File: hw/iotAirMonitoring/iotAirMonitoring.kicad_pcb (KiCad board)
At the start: 2 copper layers, 100 x 100 mm, 122 parts, among them J1 MQ-7, J10 USB_DATA, J11 PWR, J12 USB_B_Micro, J13 PM1003, J2 VEML7700, J3 SHT40, J4 PROGRAMMER, J5 ML8511, J6 EN_3V3_PROGRAMMER, J7 BMP388, J8 PMS5003, J9 USB_C_Receptacle_USB2.0, Q1 MMBT3904, Q10 AO3401A, Q11 2N7002, Q12 AO3401A, Q13 2N7002, Q14 AO3401A, Q15 2N7002, Q16 2N7002, Q17 2N7002, Q2 MMBT3904, Q3 AO3401A, Q4 2N7002, Q5 AO3401A, Q6 2N7002, Q7 AO3401A, Q8 2N7002, Q9 AO3401A, SW1 PWR_ON, SW2 PWR_OFF, SW3 RESET, SW4 SW_Push, U1 ESP32-WROOM-32, U2 MCP3202-BI/SN, U3 AMS1117-3.3, U4 TPS54331, U5 RFM95W-868S2

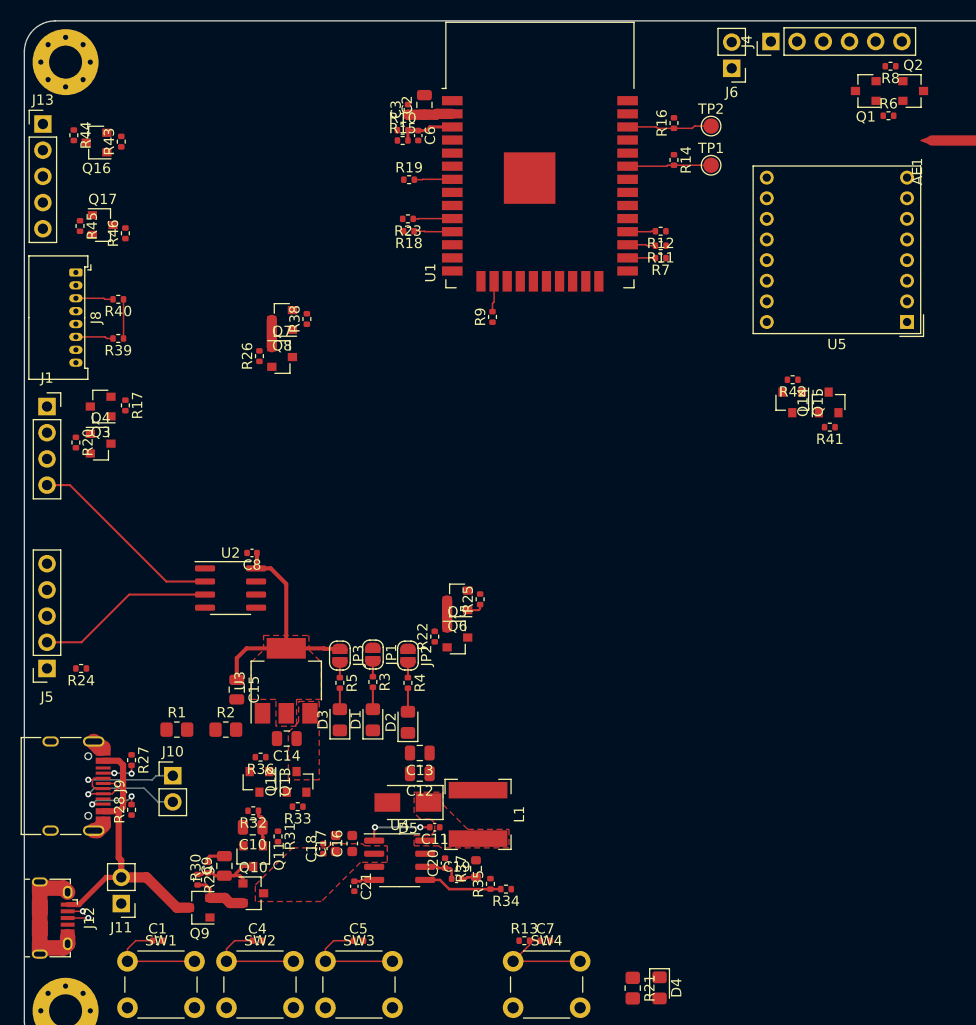
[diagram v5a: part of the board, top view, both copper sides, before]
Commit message: More routing on main board
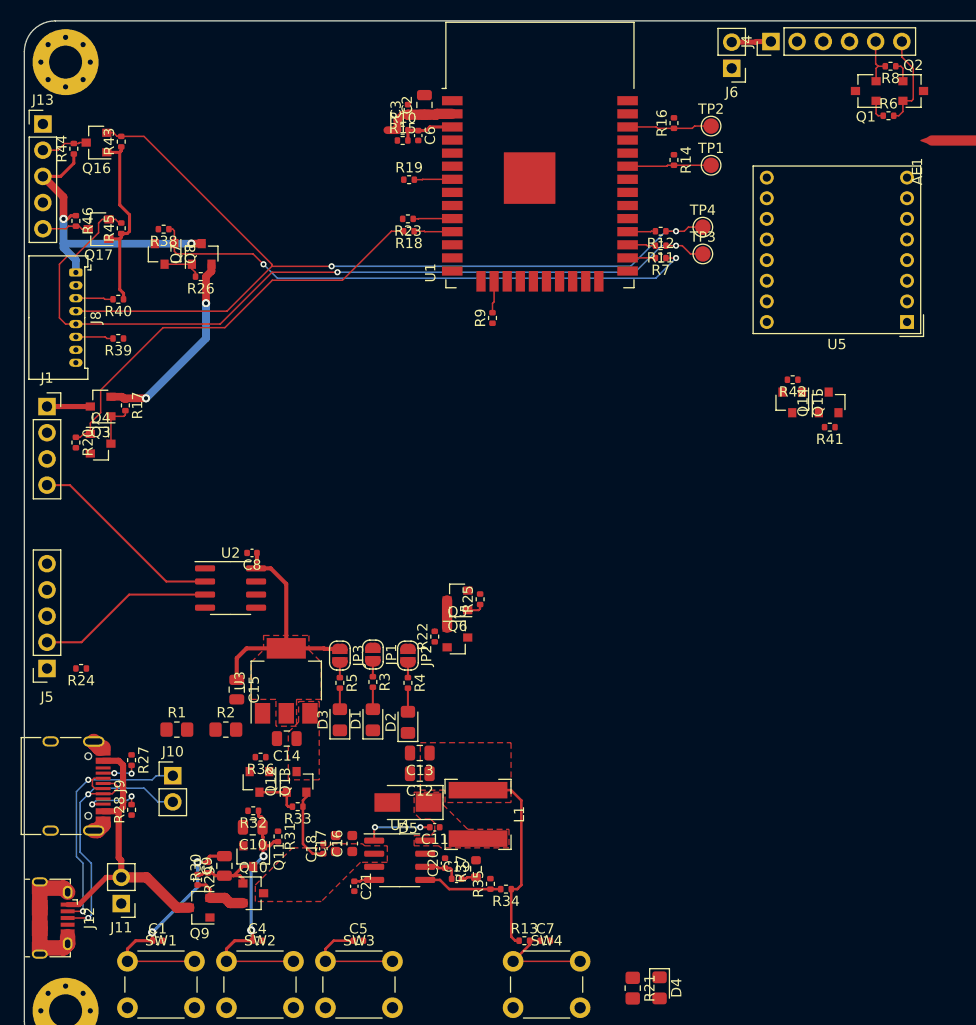
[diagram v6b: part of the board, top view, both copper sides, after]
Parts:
- added TP3: TP_RX1, TestPoint:TestPoint_Pad_D1.5mm, F.Cu at (221.8, 67.6)
- added TP4: TP_TX1, TestPoint:TestPoint_Pad_D1.5mm, F.Cu at (221.8, 65.0)
- moved R38 16.4 mm to (169.5, 65.2), turned to 180 degrees
- moved Q8 13.1 mm to (169.6, 67.6), turned to 270 degrees
- moved Q7 12.7 mm to (173.2, 67.6), turned to 90 degrees
- moved R26 9.58 mm to (173.1, 69.8), turned to 180 degrees
- moved R46 4.95 mm to (161.0, 64.4), turned to 270 degrees
- moved R45 4.01 mm to (165.4, 65.1), turned to 90 degrees
- moved R44 1.31 mm to (160.8, 57.4), turned to 90 degrees
- moved Q17 0.57 mm to (163.2, 65.2), turned to 180 degrees
- moved R9 0.10 mm to (201.4, 73.8)
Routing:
- net TX1: track 0.00 -> 86.6 mm, vias 0 -> 2
- net RX1: track 0.00 -> 80.8 mm, vias 0 -> 2
- net PMS_EN: track 0.00 -> 54.1 mm, vias 0 -> 2
- net Net-(Q4-Pad1): track 0.00 -> 42.0 mm
- net 3V3: track 8.14 -> 45.5 mm
- net DUST_VDD: track 0.00 -> 29.8 mm, vias 0 -> 2
- net VDD: track 0.00 -> 27.1 mm, vias 0 -> 2
- net D-: track 13.1 -> 26.6 mm
- net D+: track 15.8 -> 28.7 mm
- net PWR_OFF: track 14.3 -> 25.6 mm, vias 0 -> 2
- net PWR_ON: track 12.6 -> 23.0 mm, vias 0 -> 2
- net RTS: track 0.00 -> 9.22 mm
- net DTR: track 0.00 -> 4.72 mm
- net PM_RX: track 0.00 -> 4.62 mm
- net Net-(Q3-Pad1): track 0.00 -> 4.51 mm
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- added copper zone on F.Cu, net 3V3

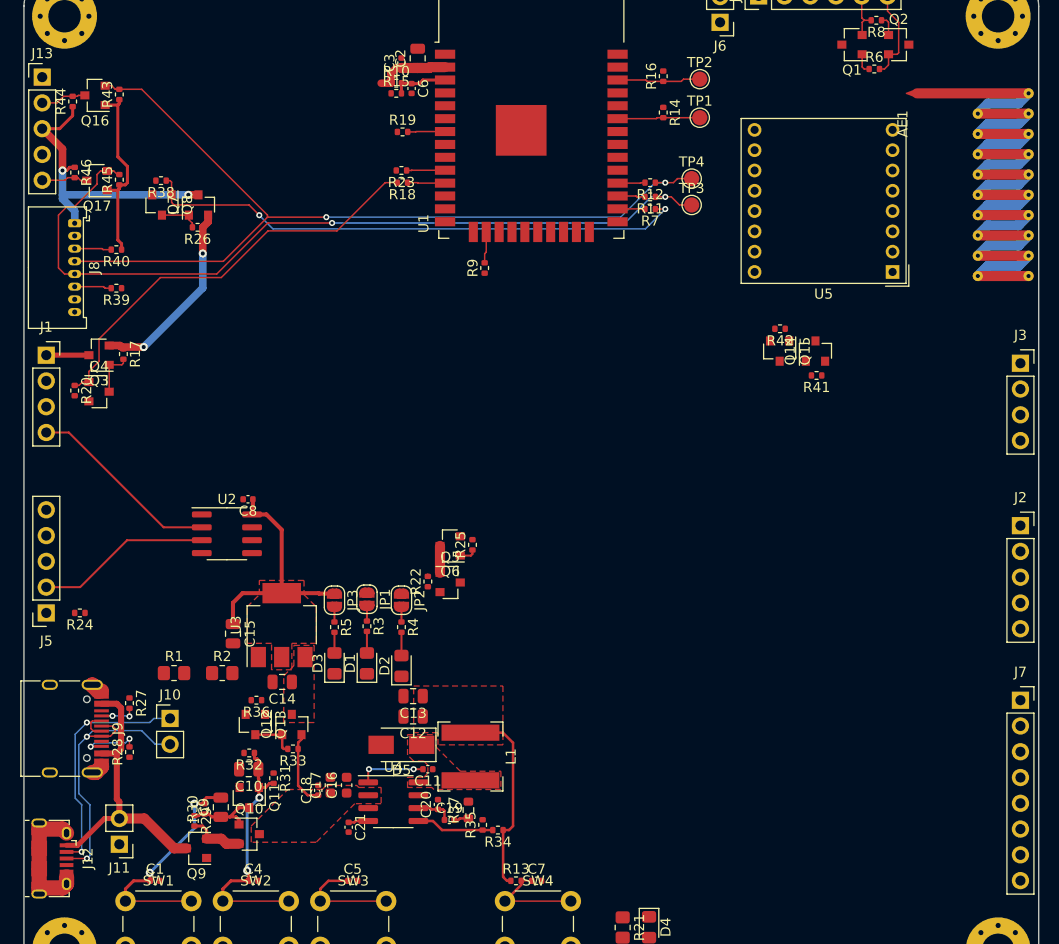
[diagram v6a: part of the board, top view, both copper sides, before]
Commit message: More routing on main board
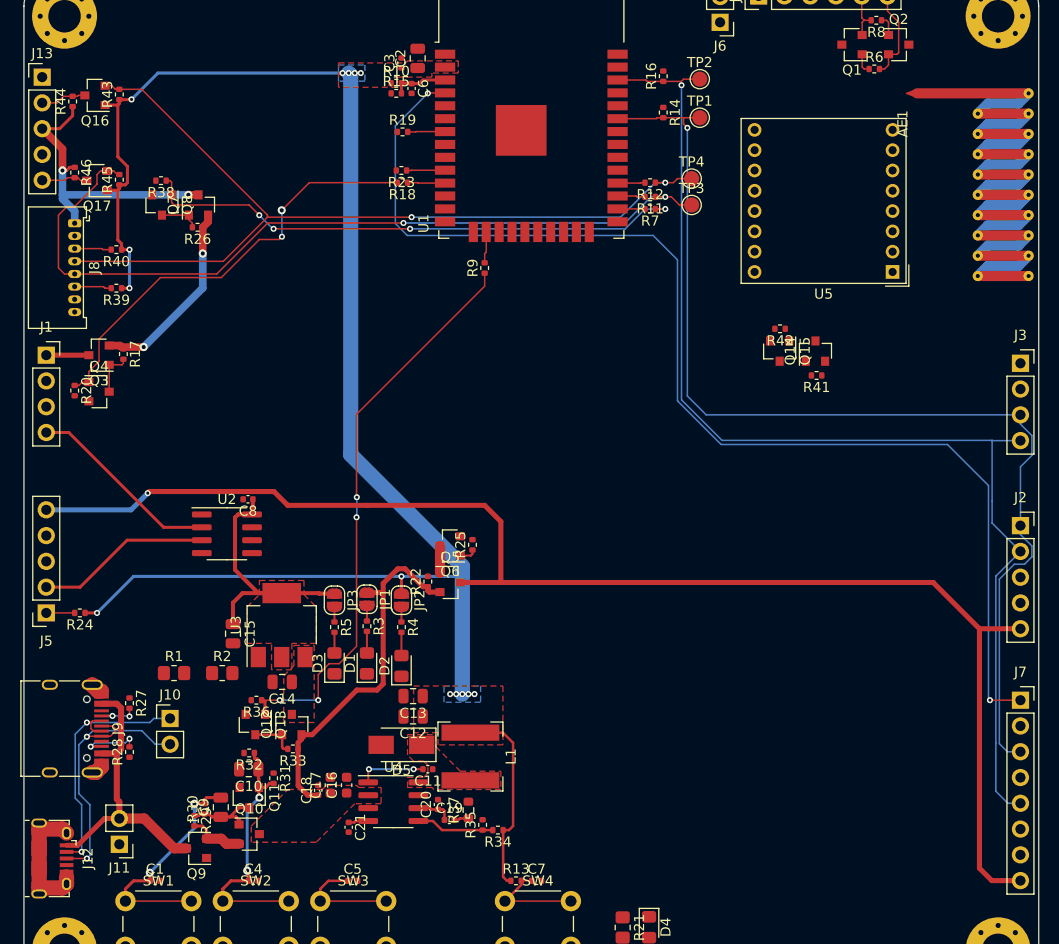
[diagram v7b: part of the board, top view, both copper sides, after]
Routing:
- net SEN_VDD: track 0.00 -> 138.0 mm, vias 0 -> 1
- net 3V3: track 45.5 -> 172.6 mm, vias 0 -> 14
- net BMP_INT: track 0.00 -> 117.4 mm, vias 0 -> 2
- net SCL: track 8.25 -> 114.4 mm, vias 0 -> 1
- net SDA: track 8.14 -> 107.4 mm, vias 0 -> 1
- net LDO_EN: track 0.00 -> 56.7 mm, vias 0 -> 4
- net VDD: track 27.1 -> 56.1 mm
- net /interface/UV_EN: track 0.00 -> 2.80 mm
- net 3V3_L: track 23.8 -> 26.5 mm
- net Net-(Q4-Pad1): track 42.0 -> 43.5 mm, vias 0 -> 2
- net PMS_EN: vias 2 -> 4
- added copper zone on B.Cu, net 3V3

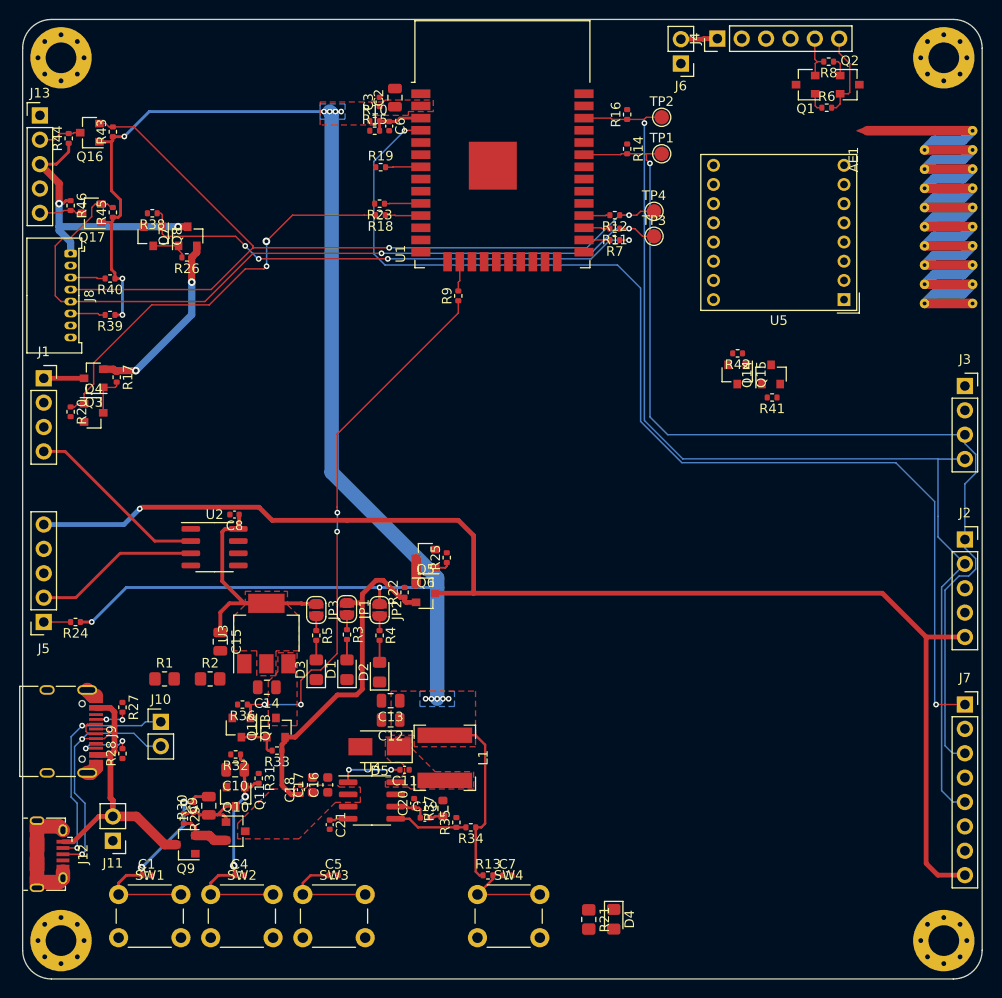
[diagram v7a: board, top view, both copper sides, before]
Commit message: First version routed main board
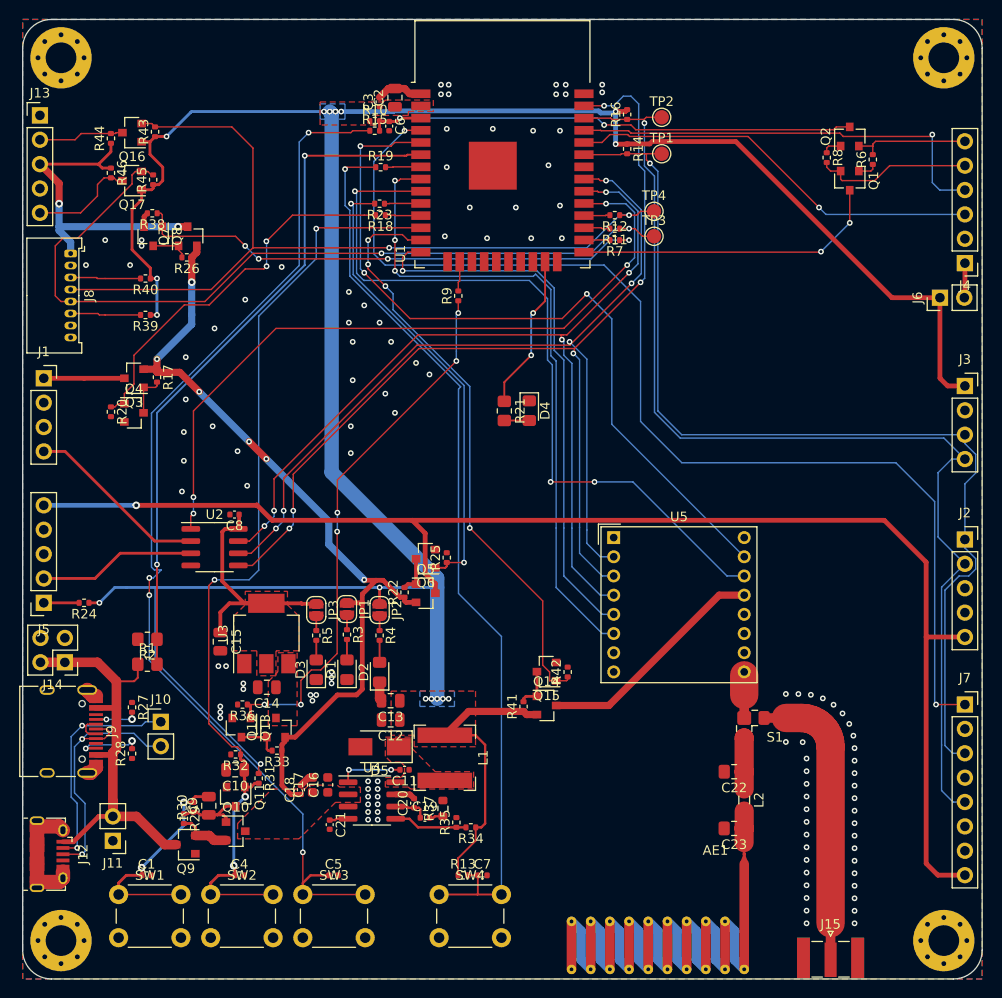
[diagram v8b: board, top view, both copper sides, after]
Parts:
- added C22: C, Capacitor_SMD:C_0805_2012Metric_Pad1.18x1.45mm_HandSolder, F.Cu at (230.2, 123.4)
- added C23: C, Capacitor_SMD:C_0805_2012Metric_Pad1.18x1.45mm_HandSolder, F.Cu at (230.1, 129.3)
- added J14: Battery_shield, Connector_PinHeader_2.54mm:PinHeader_2x02_P2.54mm_Vertical, F.Cu at (160.4, 112.0)
- added J15: SMA, Connector_Coaxial:SMA_Samtec_SMA-J-P-X-ST-EM1_EdgeMount, F.Cu at (240.2, 142.8)
- added L2: L, Inductor_SMD:L_0805_2012Metric_Pad1.05x1.20mm_HandSolder, F.Cu at (231.2, 126.3)
- added S1: RF_Splitter, iotAirMonitoring:RF_Splitter, F.Cu at (231.2, 117.8)
- moved AE1 77.5 mm to (222.2, 138.2), turned to 180 degrees
- moved R21 53.7 mm to (206.2, 85.8)
- moved D4 53.7 mm to (208.8, 85.8)
- moved Q14 41.7 mm to (210.6, 116.5), turned to 0 degrees
- moved R41 41.3 mm to (208.2, 116.6), turned to 90 degrees
- moved R42 37.6 mm to (212.8, 113.0), turned to 90 degrees
- moved Q15 36.8 mm to (210.6, 113.0), turned to 180 degrees
- moved J6 36.4 mm to (251.6, 74.0), turned to 90 degrees
- moved J4 34.8 mm to (254.2, 70.4), turned to 180 degrees
- moved U5 34.5 mm to (217.6, 99.0), turned to 0 degrees
- moved Q1 11.0 mm to (242.2, 61.8), turned to 270 degrees
- moved R8 10.0 mm to (239.8, 59.4), turned to 270 degrees
- moved R2 7.73 mm to (169.0, 109.6), turned to 180 degrees
- moved R6 7.22 mm to (244.6, 59.6), turned to 90 degrees
- moved Q17 5.40 mm to (167.4, 61.8)
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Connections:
- R1 pad 1: VDD -> USB_VDD
- U5 pad 9: Net-(AE1-Pad1) -> Net-(S1-Pad1)
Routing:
- net 3V3: track 172.6 -> 288.0 mm, vias 14 -> 17
- net MOSI: track 0.00 -> 108.9 mm, vias 0 -> 5
- net Net-(C5-Pad1): track 10.8 -> 111.6 mm, vias 0 -> 4
- net SCLK: track 0.00 -> 98.3 mm, vias 0 -> 5
- net MISO: track 0.00 -> 96.1 mm, vias 0 -> 5
- net SWITCH: track 10.2 -> 95.4 mm, vias 0 -> 1
- net DIO1: track 0.00 -> 80.3 mm, vias 0 -> 3
- net DIO0: track 0.00 -> 80.2 mm, vias 0 -> 3
- net CS: track 0.00 -> 75.4 mm, vias 0 -> 4
- net PWR_OFF: track 25.6 -> 99.8 mm, vias 2 -> 4
- net ADC_VIN: track 0.00 -> 71.5 mm, vias 0 -> 2
- net LORA_RST: track 0.00 -> 68.7 mm, vias 0 -> 3
- net LORA_EN: track 0.00 -> 61.9 mm, vias 0 -> 4
- net CS_LORA: track 0.00 -> 57.3 mm, vias 0 -> 1
- net EN: track 5.46 -> 53.0 mm, vias 0 -> 2
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- added copper zone on B.Cu, net GND
- added copper zone on F.Cu, net GND
